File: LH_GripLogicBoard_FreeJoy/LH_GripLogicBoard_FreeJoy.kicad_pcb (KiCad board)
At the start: 2 copper layers, 40.3 x 52.6 mm, 23 parts, among them J1 Conn_01x06, J2 Conn_01x06, J3 Conn_01x06, J4 Conn_01x02, J5 Conn_01x02, J6 Conn_01x07, J7 Conn_01x02, J8 Conn_01x02, U1 74HC165, U2 74HC165

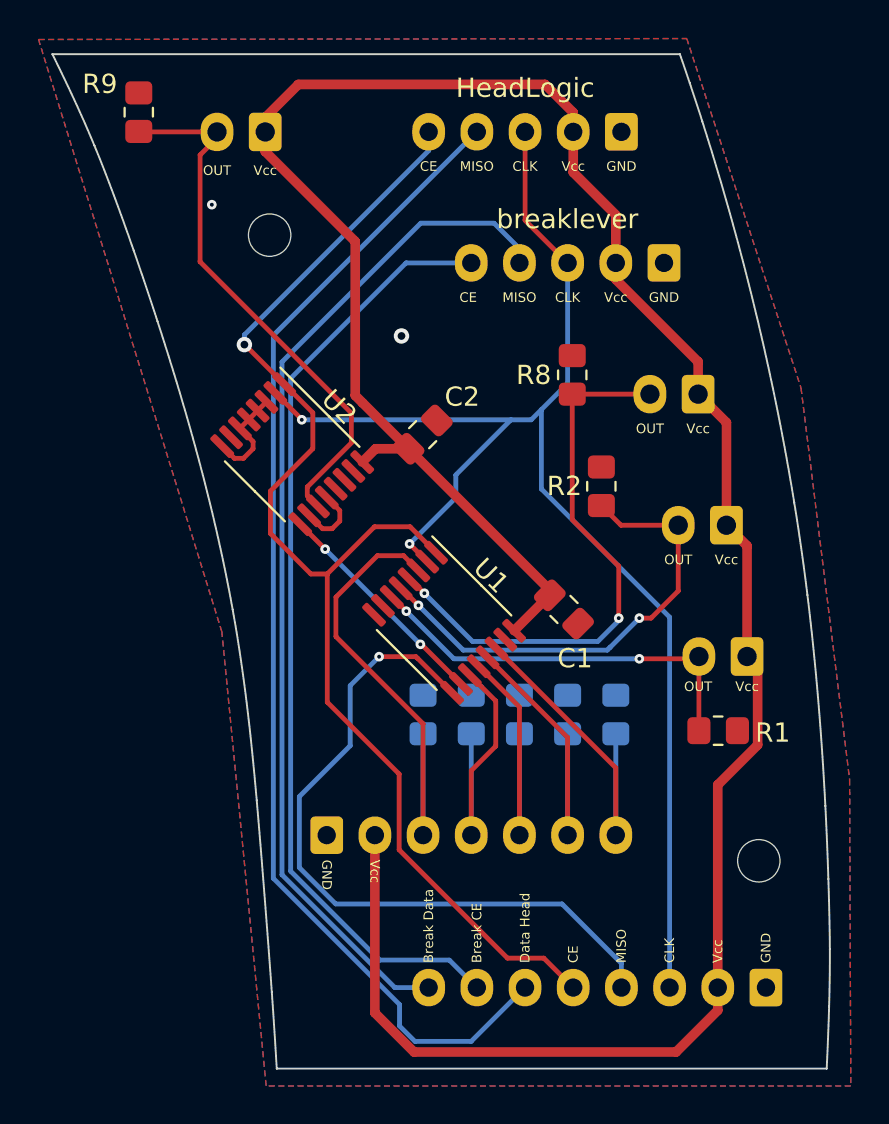
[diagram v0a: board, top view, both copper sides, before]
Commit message: fixed mistake in Grip logic pcb's
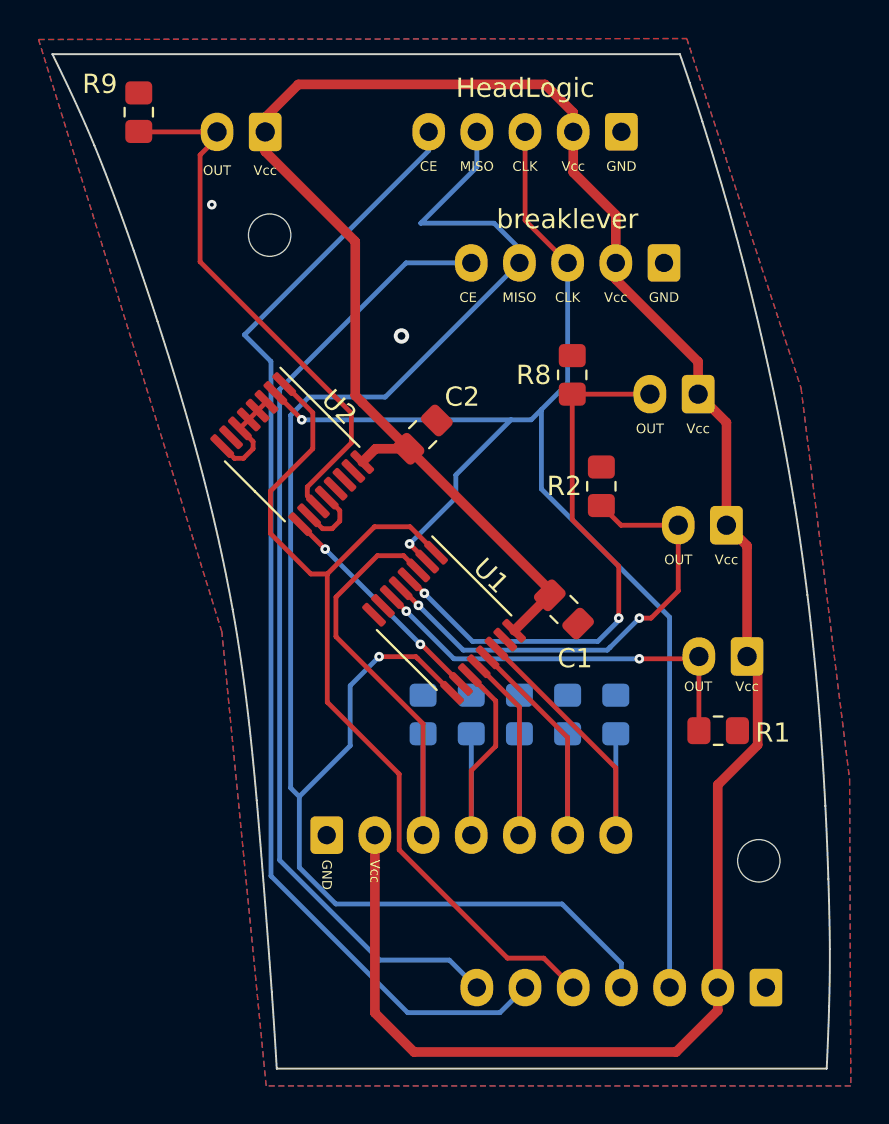
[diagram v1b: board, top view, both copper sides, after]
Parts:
- J1: footprint Connector_JST:JST_XH_B8B-XH-A_1x08_P2.50mm_Vertical -> Connector_JST:JST_XH_B7B-XH-A_1x07_P2.50mm_Vertical
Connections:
- J1 pad 5: CE -> CE_Grip
- J1 pad 6: Data_Head -> CE_HEAD
- J2 pad 4: Data_Head -> MISO
- J2 pad 5: CE -> CE_HEAD
- J3 pad 4: Data_Breaklever -> MISO
- U1 pad 1: CE -> CE_Grip
- U2 pad 1: CE -> CE_Grip
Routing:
- net CE: track 66.1 -> 0.00 mm, vias 1 -> 0
- net Data_Head: track 61.5 -> 0.00 mm
- net CE_HEAD: track 0.00 -> 59.8 mm
- net Data_Breaklever: track 53.2 -> 0.00 mm
- net CE_Grip: track 0.00 -> 48.2 mm
- net MISO: track 37.2 -> 84.7 mm
